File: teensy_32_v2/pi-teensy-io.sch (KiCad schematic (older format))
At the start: 16 parts, among them J3 CJ, J4 CJ, J5 CJ, J6 CJ, U4 PCF8563TS/5,118, Y1 SC20S-12.5PF20PPM

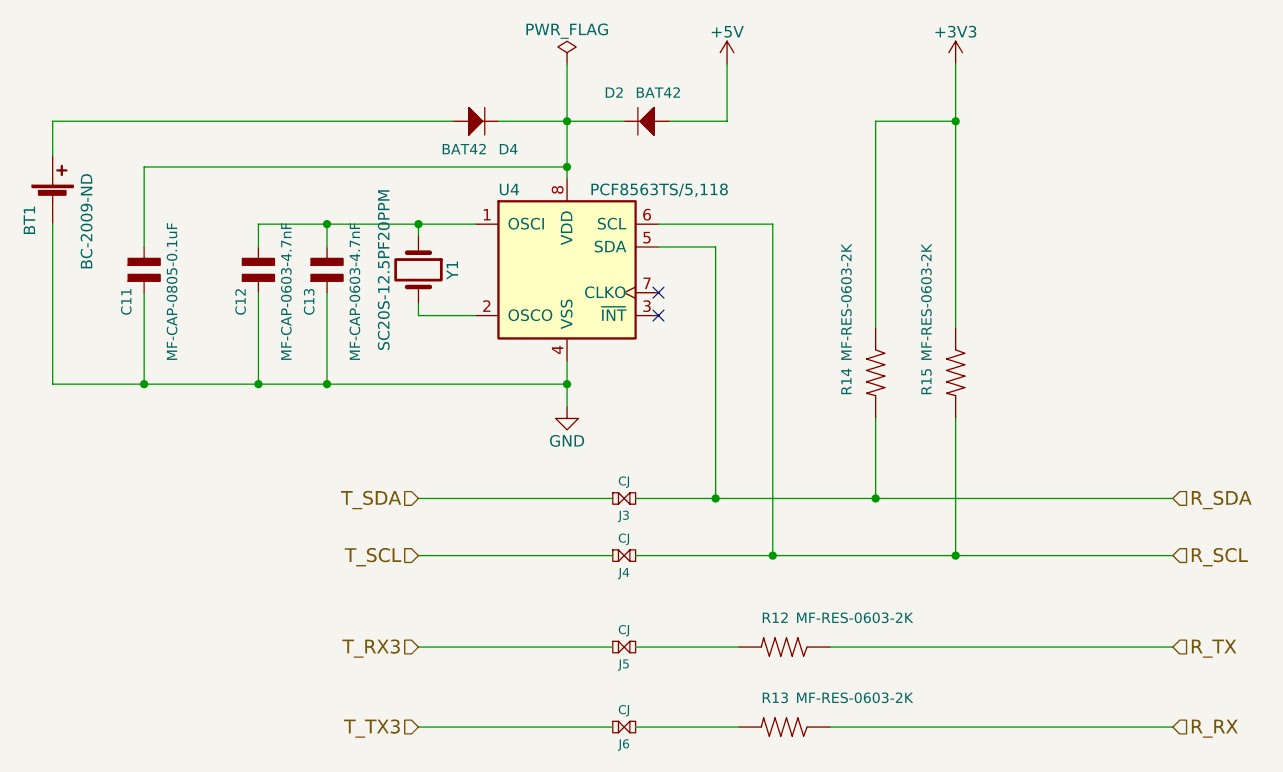
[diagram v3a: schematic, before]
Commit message: update teensy hat schematic
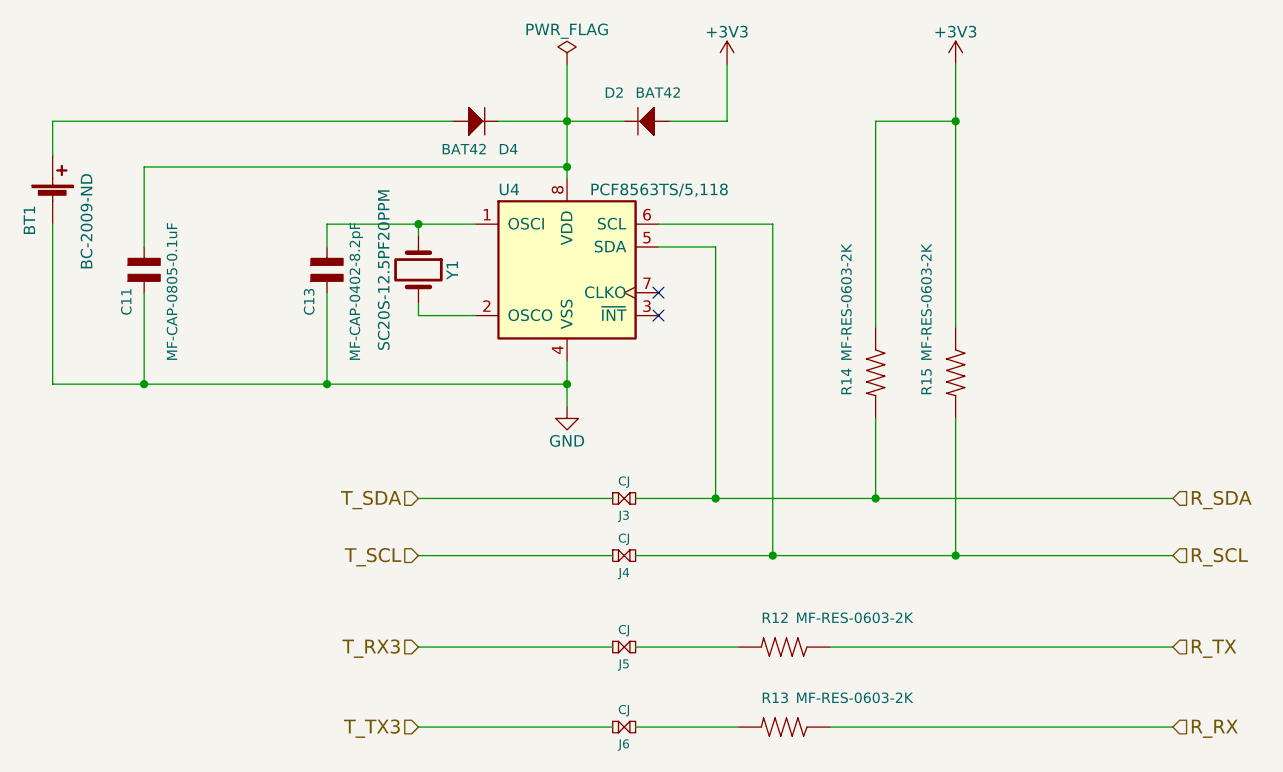
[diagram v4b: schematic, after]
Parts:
- removed C12: MF-CAP-0603-4.7nF, MF_Passives:MF_Passives-C0603, symbol CAPACITOR_NP_0805
- C13: value MF-CAP-0603-4.7nF -> MF-CAP-0402-8.2pF; footprint MF_Passives:MF_Passives-C0603 -> MF_Passives:MF_Passives-C0402
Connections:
- net +5V is gone; now on net +3V3: D2.ANOD (ANODE)
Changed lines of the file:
@@
 $EndComp
 $Comp
-L +3V3 #PWR021
+L +3V3 #PWR024
 U 1 1 59ED724A
 P 6350 950
-F 0 "#PWR021" H 6350 800 50  0001 C CNN
+F 0 "#PWR024" H 6350 800 50  0001 C CNN
 F 1 "+3V3" H 6350 1090 50  0000 C CNN
 F 2 "" H 6350 950 50  0001 C CNN
@@
 $EndComp
 $Comp
-L GND #PWR022
+L GND #PWR025
 U 1 1 59ED9DE4
 P 4650 2450
-F 0 "#PWR022" H 4650 2200 50  0001 C CNN
+F 0 "#PWR025" H 4650 2200 50  0001 C CNN
 F 1 "GND" H 4650 2300 50  0000 C CNN
 F 2 "" H 4650 2450 50  0001 C CNN
@@
 $EndComp
 $Comp
-L +5V #PWR023
-U 1 1 59EDA676
-P 5350 950
-F 0 "#PWR023" H 5350 800 50  0001 C CNN
-F 1 "+5V" H 5350 1090 50  0000 C CNN
-F 2 "" H 5350 950 50  0001 C CNN
-F 3 "" H 5350 950 50  0001 C CNN
-	1    5350 950
-	1    0    0    -1
-$EndComp
-$Comp
-L PWR_FLAG #FLG024
+L PWR_FLAG #FLG026
 U 1 1 59F89F7B
 P 4650 950
-F 0 "#FLG024" H 4650 1025 50  0001 C CNN
+F 0 "#FLG026" H 4650 1025 50  0001 C CNN
 F 1 "PWR_FLAG" H 4650 1100 50  0000 C CNN
 F 2 "" H 4650 950 50  0001 C CNN
@@
 AR Path="/59ED67C6/5A1C76F9" Ref="C13"  Part="1"
 F 0 "C13" V 3550 1650 45  0000 L BNN
-F 1 "MF-CAP-0603-4.7nF" V 3750 1450 45  0000 L BNN
-F 2 "MF_Passives:MF_Passives-C0603" H 3850 1760 20  0001 C CNN
+F 1 "MF-CAP-0402-8.2pF" V 3750 1450 45  0000 L BNN
+F 2 "MF_Passives:MF_Passives-C0402" H 3850 1760 20  0001 C CNN
 F 3 "" H 3600 1850 60  0001 C CNN
 	1    3600 1850
 	1    0    0    -1
 $EndComp
-$Comp
-L CAPACITOR_NP_0805 C?
-U 1 1 5A1C7720
-P 3300 1850
-AR Path="/59ED6513/5A1C7720" Ref="C?"  Part="1"
-AR Path="/59ED67C6/5A1C7720" Ref="C12"  Part="1"
-F 0 "C12" V 3250 1650 45  0000 L BNN
-F 1 "MF-CAP-0603-4.7nF" V 3450 1450 45  0000 L BNN
-F 2 "MF_Passives:MF_Passives-C0603" H 3550 1760 20  0001 C CNN
-F 3 "" H 3300 1850 60  0001 C CNN
-	1    3300 1850
-	1    0    0    -1
-$EndComp
 Wire Wire Line
 	4950 2850 7300 2850
@@
 Wire Wire Line
 	4000 2050 4000 2000
-Wire Wire Line
-	3300 1650 4250 1650
 Wire Wire Line
 	4000 1650 4000 1700
@@
 Connection ~ 4000 1650
 Wire Wire Line
-	3300 1750 3300 1650
-Connection ~ 3600 1650
-Wire Wire Line
 	3600 1950 3600 2350
 Connection ~ 3600 2350
 Wire Wire Line
-	3300 1950 3300 2350
-Connection ~ 3300 2350
+	3600 1650 4250 1650
+$Comp
+L +3V3 #PWR027
+U 1 1 5A46B84A
+P 5350 950
+F 0 "#PWR027" H 5350 800 50  0001 C CNN
+F 1 "+3V3" H 5350 1090 50  0000 C CNN
+F 2 "" H 5350 950 50  0001 C CNN
+F 3 "" H 5350 950 50  0001 C CNN
+	1    5350 950
+	1    0    0    -1
+$EndComp
 $EndSCHEMATC
